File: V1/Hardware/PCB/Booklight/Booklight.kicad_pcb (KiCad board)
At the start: 2 copper layers, 21 x 31 mm, 35 parts, among them J1 Alterative_charging, Q2 8205A, U1 TP4056-42-ESOP8, U3 DW01A, U7 MCP1825S, U8 LM397

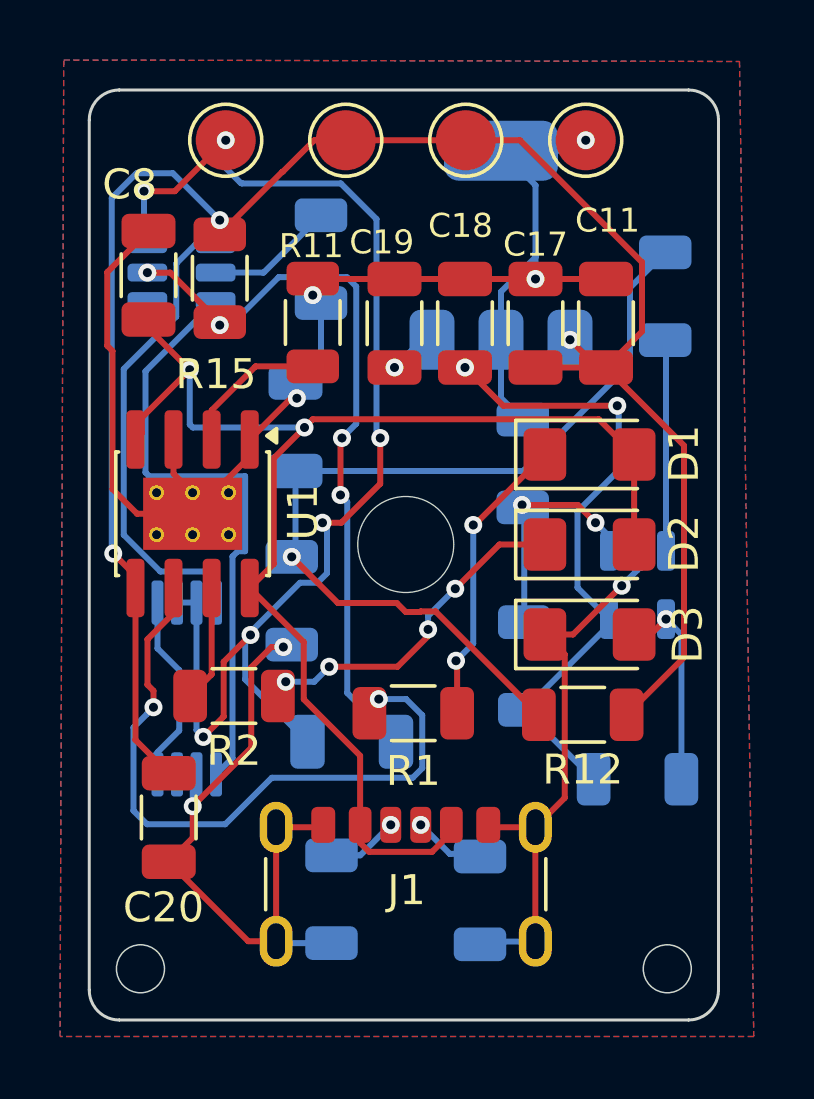
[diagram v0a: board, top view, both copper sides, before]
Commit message: Swapped comperator
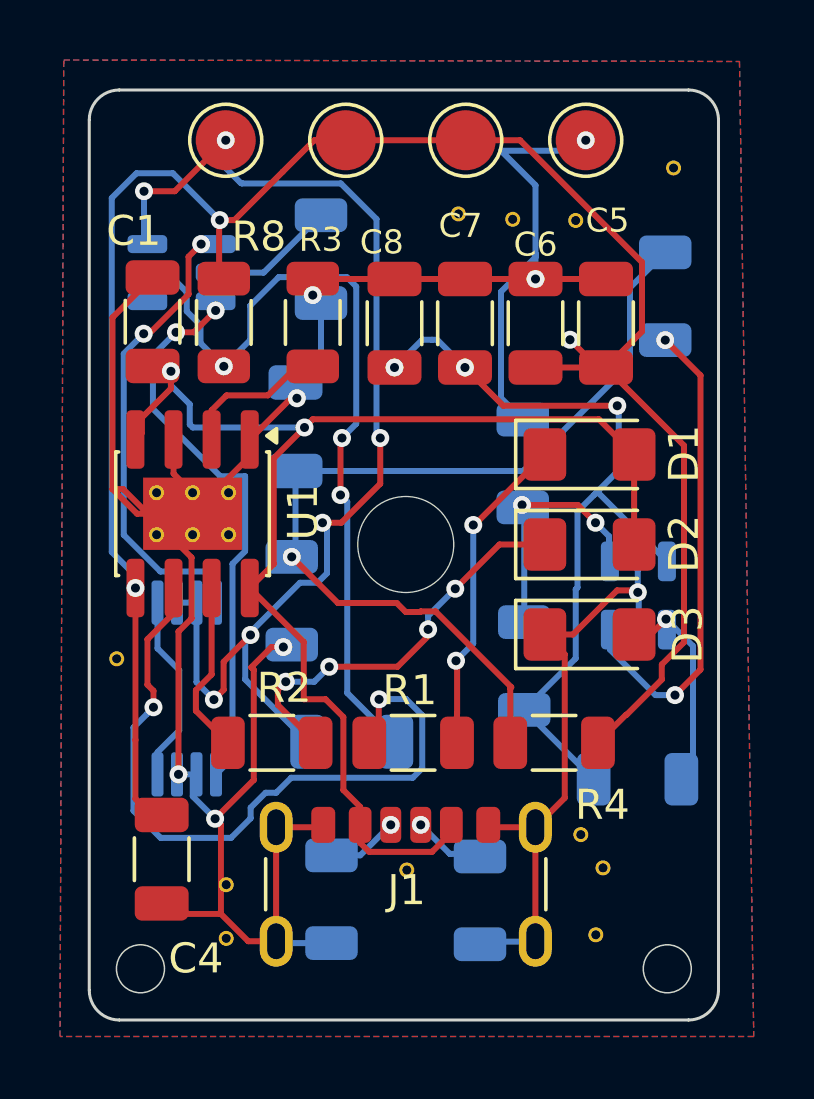
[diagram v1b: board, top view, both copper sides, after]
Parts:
- removed U7: MCP1825S, Package_TO_SOT_SMD:SOT-223-3_TabPin2
- removed U8: LM397, Package_TO_SOT_SMD:SOT-23-5
- added ?: , , F.Cu at (76.6, 68.8)
- added ?: , , F.Cu at (76.4, 48.3)
- added ?: , , F.Cu at (70.8, 70.0)
- added ?: , , F.Cu at (74.3, 48.3)
- added ?: , , F.Cu at (79.7, 46.5)
- added ?: , , F.Cu at (64.8, 70.4)
- added ?: , , F.Cu at (61.1, 62.9)
- added ?: , , F.Cu at (77.1, 72.1)
- added ?: , , F.Cu at (72.5, 48.1)
- added ?: , , F.Cu at (64.8, 72.2)
- added ?: , , F.Cu at (77.3, 69.9)
- added U3: TLV7041DBV, Package_TO_SOT_SMD:SOT-23-5, B.Cu at (78.5, 60.8)
- R3: renamed from R11; value 1k -> 2k
- moved R2 2.01 mm to (66.3, 65.7)
- moved C1 1.56 mm to (62.3, 51.7)
- moved R8 1.48 mm to (64.7, 51.7)
- moved C4 1.41 mm to (62.6, 69.6)
- moved R4 1.34 mm to (75.7, 65.7)
- moved R1 0.99 mm to (71.0, 65.7)
- renumbered C8 to C1, C12 to C2, C13 to C3, C20 to C4, C11 to C5, C17 to C6, C18 to C7, C19 to C8, Q2 to Q1, R16 to R10, R20 to R11, R22 to R12, R21 to R13, R12 to R4, R13 to R5, R14 to R6, R19 to R7, R15 to R8, R17 to R9, U3 to U2
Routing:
- net GND: track 88.9 -> 100.8 mm, vias 7 -> 8
- net Net-(U3-+): track 7.04 -> 16.2 mm, vias 0 -> 2
- net Vbat: track 63.0 -> 67.7 mm
- net Net-(U2-VCC): track 24.6 -> 27.3 mm, vias 4 -> 3
- net 3.3V: track 24.3 -> 26.8 mm
- net /Bat-: track 42.2 -> 39.7 mm
- net Net-(U1-~{STDBY}): track 22.2 -> 24.3 mm
- net Net-(D2-K): track 11.5 -> 13.6 mm
- net Net-(U1-~{CHRG}): track 3.90 -> 5.82 mm
- net Net-(Q1-G2): track 20.5 -> 18.8 mm, vias 0 -> 2
- net Vbus: track 45.5 -> 44.1 mm
- net Net-(D1-K): track 9.89 -> 10.9 mm
- net /Battery_state: track 30.2 -> 30.8 mm
- net Net-(Q1-G1): track 15.7 -> 15.9 mm, vias 0 -> 2

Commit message: Mid-work backup
I believe some minor improvements can be made to the bottom layer of the PCB
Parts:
- removed ? (x11): , 
- added G***: LOGO, Logo_footprint:Logo_5_3, F.Cu at (78.7, 70.8)
- added G***: LOGO, Logo_footprint:Logo_7_7, B.Cu at (73.5, 50.3)
- moved R11 4.53 mm to (74.0, 66.5)
- moved R13 1.97 mm to (74.7, 58.4)
- moved R10 0.97 mm to (79.7, 49.9)
- moved C3 0.87 mm to (69.3, 66.5)
- moved R12 0.10 mm to (74.7, 63.0)
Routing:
- net Net-(U1-~{STDBY}): track 24.3 -> 19.0 mm
- net /Battery_state: track 30.8 -> 35.7 mm
- net Net-(D3-A): track 7.15 -> 10.9 mm
- net /Ref: track 7.66 -> 4.69 mm, vias 2 -> 0
- net GND: track 100.8 -> 98.3 mm, vias 8 -> 22
- net Vbus: track 44.1 -> 45.6 mm
- net Vbat: track 67.7 -> 67.1 mm, vias 3 -> 2
- net /Bat-: track 39.7 -> 40.3 mm
- net Net-(U3-+): track 16.2 -> 16.7 mm
- net 3.3V: track 26.8 -> 26.9 mm, vias 3 -> 5

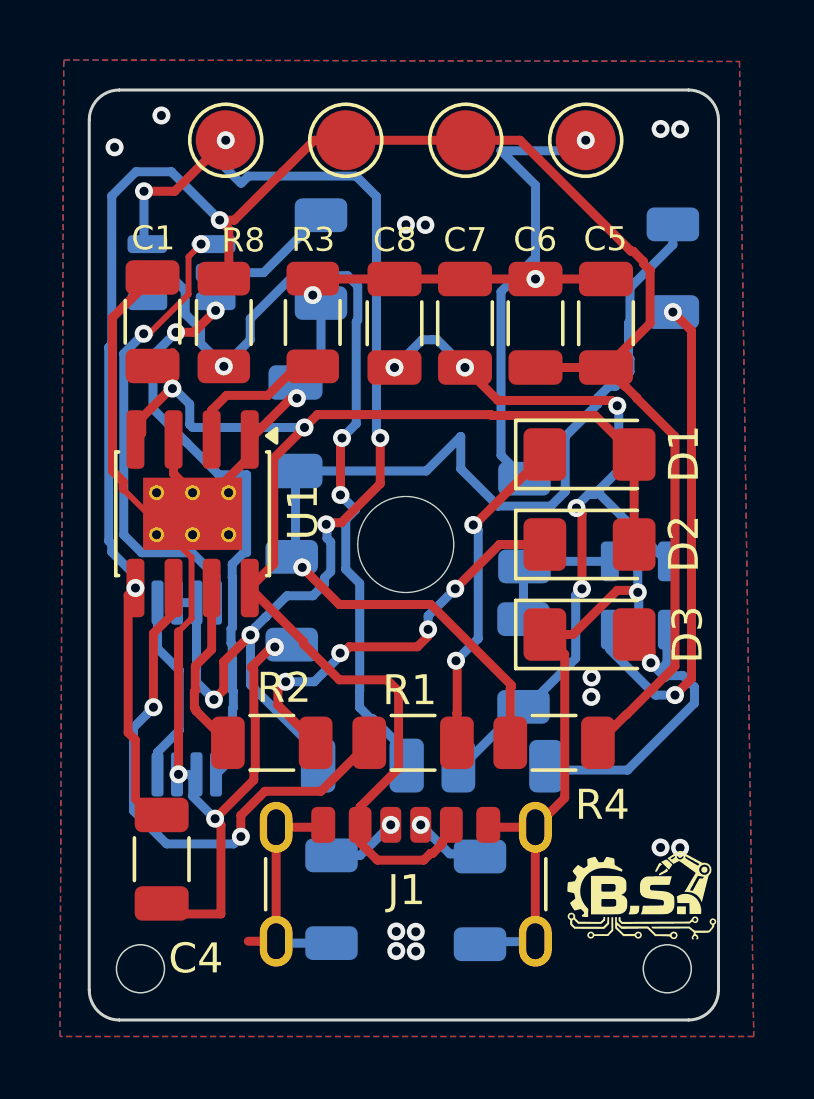
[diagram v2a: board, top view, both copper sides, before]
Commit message: Add 3.3V regulator to PCB
This change adds an MCP1825S LDO footprint and routes the 3.3V rail through the updated power network. It also updates board copper, via placement, net assignments, and KiCad metadata/UUIDs to match the revised layout and component placement.
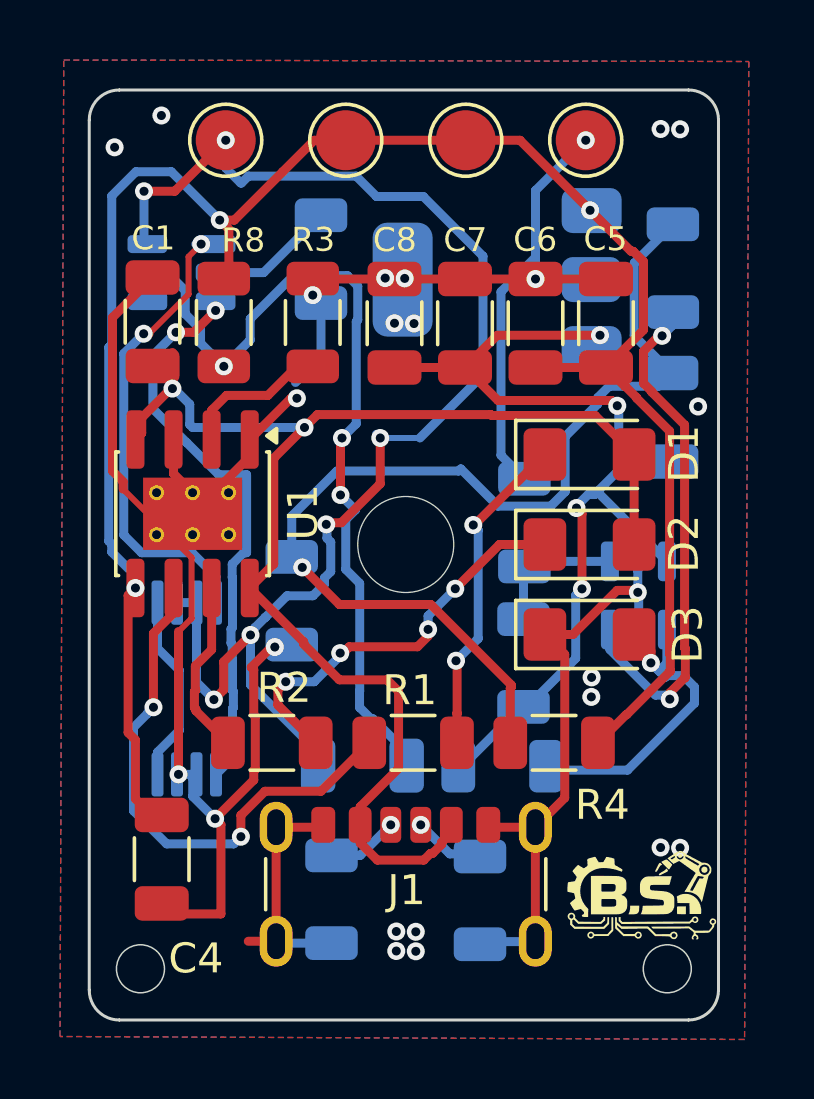
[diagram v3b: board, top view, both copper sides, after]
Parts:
- added U4: MCP1825S, Package_TO_SOT_SMD:SOT-223-3_TabPin2, B.Cu at (73.8, 50.3)
- moved C2 12.5 mm to (79.6, 54.9), turned to -90 degrees
- moved G*** 10.1 mm to (65.1, 55.9), turned to 90 degrees
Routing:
- net /Bat-: track 40.3 -> 45.0 mm
- net 3.3V: track 26.9 -> 31.0 mm, vias 5 -> 4
- net Net-(U3-+): track 16.7 -> 17.5 mm
- net GND: track 98.3 -> 97.8 mm, vias 22 -> 25
- net Vbat: track 67.1 -> 66.8 mm, vias 2 -> 3
